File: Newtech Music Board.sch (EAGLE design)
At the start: 55 parts, among them IC1 LM386N-1, J1 SS-30_BOARD_CONNECTOR, J2 MJ-3502N, U1 74LS10N, U2 74LS174N, U3 4050N, U4 4069N, U6 78L05

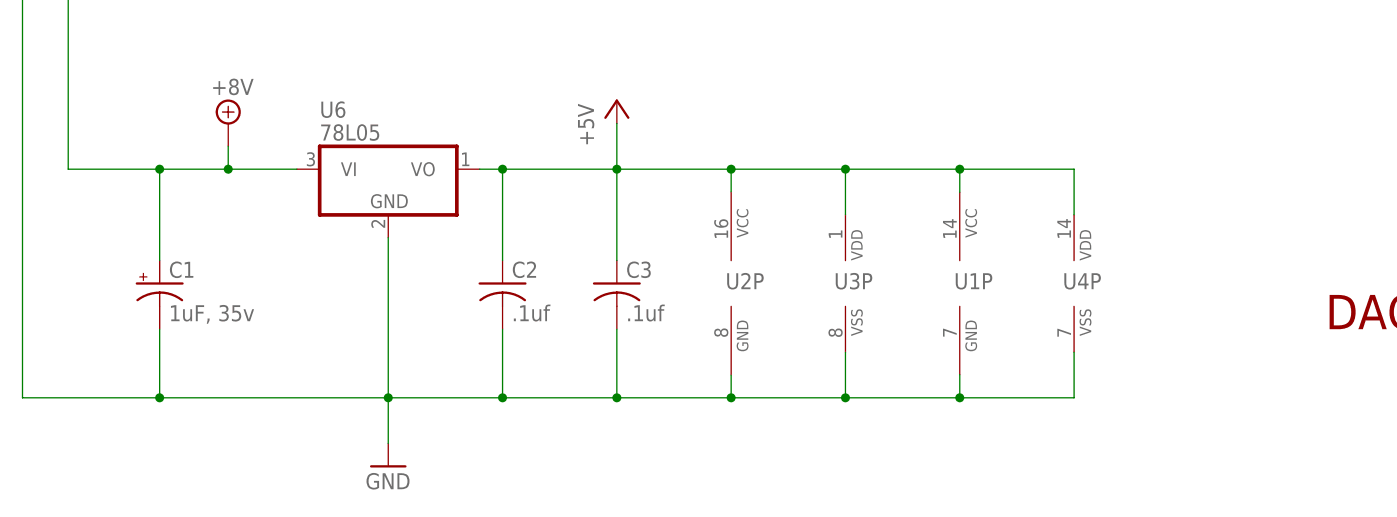
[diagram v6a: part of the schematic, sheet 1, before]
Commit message: Redid the DAC routing
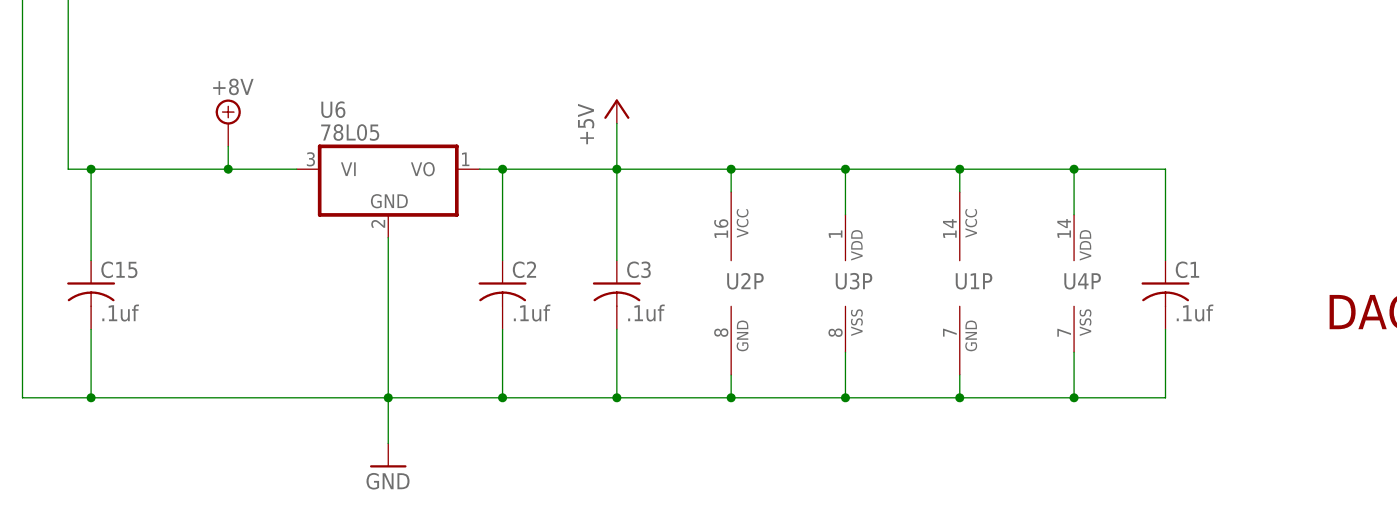
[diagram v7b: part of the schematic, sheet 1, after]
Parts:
- added C15: .1uf, rcl:C-US025-025X050
- C1: value 1uF, 35v -> .1uf; device rcl:CPOL-USE2.5-6 -> rcl:C-US025-025X050
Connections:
- net +5V: now also C1.1
- net +8V: now also C15.1; no longer C1.+
- net GND: now also C1.2, C15.2; no longer C1.-
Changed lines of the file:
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@@
 <part name="SUPPLY1" library="supply2" deviceset="+8V" device=""/>
 <part name="SUPPLY2" library="supply2" deviceset="+8V" device=""/>
-<part name="C1" library="rcl" deviceset="CPOL-US" device="E2.5-6" value="1uF, 35v"/>
 <part name="C2" library="rcl" deviceset="C-US" device="025-025X050" value=".1uf"/>
 <part name="C3" library="rcl" deviceset="C-US" device="025-025X050" value=".1uf"/>
@@
 <part name="IC1" library="linear" library_urn="urn:adsk.eagle:library:262" deviceset="LM386?-*" device="N" package3d_urn="urn:adsk.eagle:package:16409/2" technology="1"/>
 <part name="C11" library="rcl" library_urn="urn:adsk.eagle:library:334" deviceset="CPOL-US" device="E2.5-6" package3d_urn="urn:adsk.eagle:package:23349/1" value="10uF,16V"/>
+<part name="C15" library="rcl" deviceset="C-US" device="025-025X050" value=".1uf"/>
+<part name="C1" library="rcl" deviceset="C-US" device="025-025X050" value=".1uf"/>
 </parts>
 <sheets>
@@
 <attribute name="VALUE" x="28.575" y="53.975" size="1.778" layer="96"/>
 </instance>
-<instance part="C1" gate="G$1" x="22.86" y="33.02" smashed="yes">
-<attribute name="NAME" x="23.876" y="33.655" size="1.778" layer="95"/>
-<attribute name="VALUE" x="23.876" y="28.829" size="1.778" layer="96"/>
-</instance>
 <instance part="C2" gate="G$1" x="60.96" y="33.02" smashed="yes">
 <attribute name="NAME" x="61.976" y="33.655" size="1.778" layer="95"/>
@@
 <attribute name="NAME" x="40.630440625" y="51.44535" size="1.78023125" layer="95"/>
 <attribute name="VALUE" x="40.626940625" y="48.904790625" size="1.78105" layer="96"/>
+</instance>
+<instance part="C15" gate="G$1" x="15.24" y="33.02" smashed="yes">
+<attribute name="NAME" x="16.256" y="33.655" size="1.778" layer="95"/>
+<attribute name="VALUE" x="16.256" y="28.829" size="1.778" layer="96"/>
+</instance>
+<instance part="C1" gate="G$1" x="134.62" y="33.02" smashed="yes">
+<attribute name="NAME" x="135.636" y="33.655" size="1.778" layer="95"/>
+<attribute name="VALUE" x="135.636" y="28.829" size="1.778" layer="96"/>
 </instance>
 </instances>
@@
 <wire x1="15.24" y1="111.76" x2="12.7" y2="111.76" width="0.1524" layer="91"/>
 <wire x1="12.7" y1="111.76" x2="12.7" y2="45.72" width="0.1524" layer="91"/>
-<wire x1="12.7" y1="45.72" x2="22.86" y2="45.72" width="0.1524" layer="91"/>
+<wire x1="12.7" y1="45.72" x2="15.24" y2="45.72" width="0.1524" layer="91"/>
 <pinref part="J1" gate="G$2" pin="+8V@1"/>
-<wire x1="22.86" y1="45.72" x2="30.48" y2="45.72" width="0.1524" layer="91"/>
+<wire x1="15.24" y1="45.72" x2="30.48" y2="45.72" width="0.1524" layer="91"/>
 <wire x1="15.24" y1="114.3" x2="12.7" y2="114.3" width="0.1524" layer="91"/>
 <wire x1="12.7" y1="114.3" x2="12.7" y2="111.76" width="0.1524" layer="91"/>
@@
 <pinref part="SUPPLY2" gate="+8V" pin="+8V"/>
 <wire x1="30.48" y1="48.26" x2="30.48" y2="45.72" width="0.1524" layer="91"/>
-<pinref part="C1" gate="G$1" pin="+"/>
-<wire x1="22.86" y1="45.72" x2="22.86" y2="35.56" width="0.1524" layer="91"/>
-<junction x="22.86" y="45.72"/>
 <pinref part="U6" gate="G$1" pin="VI"/>
 <wire x1="30.48" y1="45.72" x2="38.1" y2="45.72" width="0.1524" layer="91"/>
 <junction x="30.48" y="45.72"/>
+<pinref part="C15" gate="G$1" pin="1"/>
+<wire x1="15.24" y1="35.56" x2="15.24" y2="45.72" width="0.1524" layer="91"/>
+<junction x="15.24" y="45.72"/>
 </segment>
 <segment>
@@
 <wire x1="60.96" y1="45.72" x2="58.42" y2="45.72" width="0.1524" layer="91"/>
 <junction x="60.96" y="45.72"/>
+<pinref part="C1" gate="G$1" pin="1"/>
+<wire x1="124.46" y1="45.72" x2="134.62" y2="45.72" width="0.1524" layer="91"/>
+<wire x1="134.62" y1="45.72" x2="134.62" y2="35.56" width="0.1524" layer="91"/>
+<junction x="124.46" y="45.72"/>
 </segment>
 <segment>
@@
 </segment>
 </net>
-<net name="GND" class="0">
+<net name="GND" class="1">
 <segment>
 <pinref part="R12" gate="G$1" pin="1"/>
@@
 <wire x1="7.62" y1="109.22" x2="7.62" y2="106.68" width="0.1524" layer="91"/>
 <wire x1="7.62" y1="106.68" x2="7.62" y2="20.32" width="0.1524" layer="91"/>
-<wire x1="7.62" y1="20.32" x2="22.86" y2="20.32" width="0.1524" layer="91"/>
 <pinref part="J1" gate="G$2" pin="GND@2"/>
-<wire x1="22.86" y1="20.32" x2="48.26" y2="20.32" width="0.1524" layer="91"/>
+<wire x1="7.62" y1="20.32" x2="15.24" y2="20.32" width="0.1524" layer="91"/>
+<wire x1="15.24" y1="20.32" x2="48.26" y2="20.32" width="0.1524" layer="91"/>
 <wire x1="15.24" y1="106.68" x2="7.62" y2="106.68" width="0.1524" layer="91"/>
 <junction x="7.62" y="106.68"/>
@@
 <wire x1="99.06" y1="20.32" x2="111.76" y2="20.32" width="0.1524" layer="91"/>
 <wire x1="86.36" y1="22.86" x2="86.36" y2="20.32" width="0.1524" layer="91"/>
-<pinref part="C1" gate="G$1" pin="-"/>
-<wire x1="22.86" y1="20.32" x2="22.86" y2="27.94" width="0.1524" layer="91"/>
 <pinref part="C2" gate="G$1" pin="2"/>
 <wire x1="60.96" y1="27.94" x2="60.96" y2="20.32" width="0.1524" layer="91"/>
 <pinref part="C3" gate="G$1" pin="2"/>
 <wire x1="73.66" y1="27.94" x2="73.66" y2="20.32" width="0.1524" layer="91"/>
-<junction x="22.86" y="20.32"/>
 <junction x="48.26" y="20.32"/>
 <junction x="60.96" y="20.32"/>
@@
 <pinref part="U6" gate="G$1" pin="GND"/>
 <wire x1="48.26" y1="38.1" x2="48.26" y2="20.32" width="0.1524" layer="91"/>
+<pinref part="C15" gate="G$1" pin="2"/>
+<wire x1="15.24" y1="27.94" x2="15.24" y2="20.32" width="0.1524" layer="91"/>
+<junction x="15.24" y="20.32"/>
+<pinref part="C1" gate="G$1" pin="2"/>
+<wire x1="134.62" y1="27.94" x2="134.62" y2="20.32" width="0.1524" layer="91"/>
+<wire x1="134.62" y1="20.32" x2="124.46" y2="20.32" width="0.1524" layer="91"/>
+<junction x="124.46" y="20.32"/>
 </segment>
 </net>
@@
 </busses>
 <nets>
-<net name="GND" class="0">
+<net name="GND" class="1">
 <segment>
 <wire x1="30.48" y1="58.42" x2="33.02" y2="55.88" width="0.1524" layer="91"/>

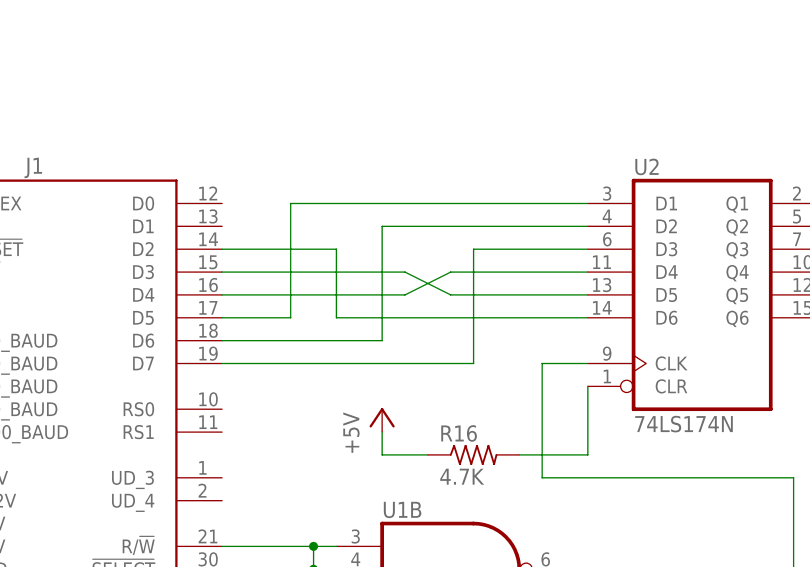
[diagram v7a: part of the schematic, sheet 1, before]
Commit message: Fixed the mixed up D7 and D5 lines
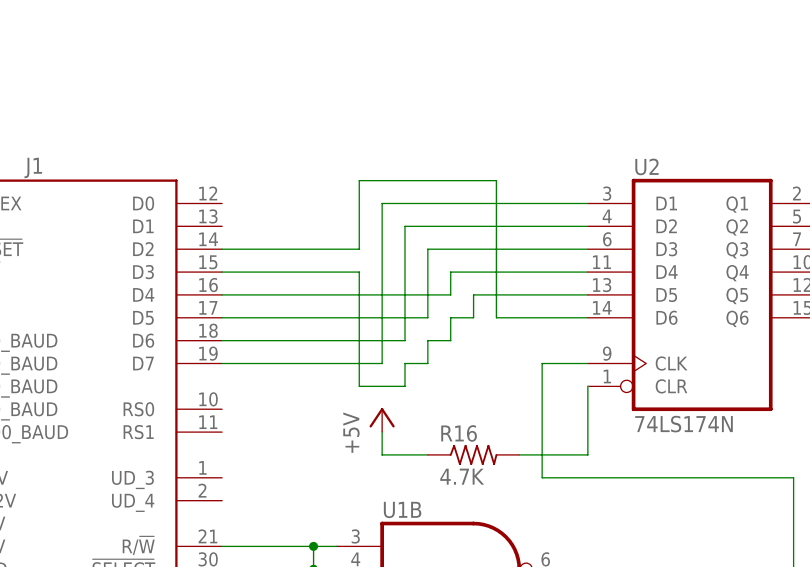
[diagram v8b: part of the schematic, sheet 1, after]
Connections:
- net N$1: now also U2A.D1; no longer U2A.D3
- net N$3: now also U2A.D3; no longer U2A.D1
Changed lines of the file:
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@@
-</segment>
-</net>
-<net name="N$1" class="0">
-<segment>
-<pinref part="U2" gate="A" pin="D3"/>
-<pinref part="J1" gate="G$2" pin="D7"/>
-<wire x1="91.44" y1="144.78" x2="78.74" y2="144.78" width="0.1524" layer="91"/>
-<wire x1="78.74" y1="144.78" x2="78.74" y2="132.08" width="0.1524" layer="91"/>
-<wire x1="78.74" y1="132.08" x2="50.8" y2="132.08" width="0.1524" layer="91"/>
-</segment>
-</net>
-<net name="N$2" class="0">
-<segment>
-<pinref part="U2" gate="A" pin="D2"/>
-<pinref part="J1" gate="G$2" pin="D6"/>
-<wire x1="91.44" y1="147.32" x2="68.58" y2="147.32" width="0.1524" layer="91"/>
-<wire x1="68.58" y1="147.32" x2="68.58" y2="134.62" width="0.1524" layer="91"/>
-<wire x1="68.58" y1="134.62" x2="50.8" y2="134.62" width="0.1524" layer="91"/>
-</segment>
-</net>
-<net name="N$3" class="0">
-<segment>
-<pinref part="U2" gate="A" pin="D1"/>
-<pinref part="J1" gate="G$2" pin="D5"/>
-<wire x1="91.44" y1="149.86" x2="58.42" y2="149.86" width="0.1524" layer="91"/>
-<wire x1="58.42" y1="149.86" x2="58.42" y2="137.16" width="0.1524" layer="91"/>
-<wire x1="58.42" y1="137.16" x2="50.8" y2="137.16" width="0.1524" layer="91"/>
-</segment>
-</net>
-<net name="N$6" class="0">
-<segment>
-<pinref part="U2" gate="A" pin="D4"/>
-<pinref part="J1" gate="G$2" pin="D4"/>
-<wire x1="91.44" y1="142.24" x2="76.2" y2="142.24" width="0.1524" layer="91"/>
-<wire x1="76.2" y1="142.24" x2="71.12" y2="139.7" width="0.1524" layer="91"/>
-<wire x1="71.12" y1="139.7" x2="50.8" y2="139.7" width="0.1524" layer="91"/>
-</segment>
-</net>
-<net name="N$7" class="0">
-<segment>
-<pinref part="U2" gate="A" pin="D5"/>
-<pinref part="J1" gate="G$2" pin="D3"/>
-<wire x1="91.44" y1="139.7" x2="76.2" y2="139.7" width="0.1524" layer="91"/>
-<wire x1="76.2" y1="139.7" x2="71.12" y2="142.24" width="0.1524" layer="91"/>
-<wire x1="71.12" y1="142.24" x2="50.8" y2="142.24" width="0.1524" layer="91"/>
-</segment>
-</net>
-<net name="N$8" class="0">
-<segment>
-<pinref part="U2" gate="A" pin="D6"/>
-<pinref part="J1" gate="G$2" pin="D2"/>
-<wire x1="91.44" y1="137.16" x2="63.5" y2="137.16" width="0.1524" layer="91"/>
-<wire x1="63.5" y1="137.16" x2="63.5" y2="144.78" width="0.1524" layer="91"/>
-<wire x1="63.5" y1="144.78" x2="50.8" y2="144.78" width="0.1524" layer="91"/>
 </segment>
 </net>
@@
 </segment>
 </net>
+<net name="N$1" class="0">
+<segment>
+<pinref part="J1" gate="G$2" pin="D7"/>
+<wire x1="50.8" y1="132.08" x2="68.58" y2="132.08" width="0.1524" layer="91"/>
+<wire x1="68.58" y1="132.08" x2="68.58" y2="149.86" width="0.1524" layer="91"/>
+<pinref part="U2" gate="A" pin="D1"/>
+<wire x1="68.58" y1="149.86" x2="91.44" y2="149.86" width="0.1524" layer="91"/>
+</segment>
+</net>
+<net name="N$2" class="0">
+<segment>
+<pinref part="J1" gate="G$2" pin="D6"/>
+<wire x1="50.8" y1="134.62" x2="71.12" y2="134.62" width="0.1524" layer="91"/>
+<wire x1="71.12" y1="134.62" x2="71.12" y2="147.32" width="0.1524" layer="91"/>
+<pinref part="U2" gate="A" pin="D2"/>
+<wire x1="71.12" y1="147.32" x2="91.44" y2="147.32" width="0.1524" layer="91"/>
+</segment>
+</net>
+<net name="N$3" class="0">
+<segment>
+<pinref part="J1" gate="G$2" pin="D5"/>
+<wire x1="50.8" y1="137.16" x2="73.66" y2="137.16" width="0.1524" layer="91"/>
+<wire x1="73.66" y1="137.16" x2="73.66" y2="144.78" width="0.1524" layer="91"/>
+<pinref part="U2" gate="A" pin="D3"/>
+<wire x1="73.66" y1="144.78" x2="91.44" y2="144.78" width="0.1524" layer="91"/>
+</segment>
+</net>
+<net name="N$6" class="0">
+<segment>
+<pinref part="J1" gate="G$2" pin="D4"/>
+<wire x1="50.8" y1="139.7" x2="76.2" y2="139.7" width="0.1524" layer="91"/>
+<wire x1="76.2" y1="139.7" x2="76.2" y2="142.24" width="0.1524" layer="91"/>
+<pinref part="U2" gate="A" pin="D4"/>
+<wire x1="76.2" y1="142.24" x2="91.44" y2="142.24" width="0.1524" layer="91"/>
+</segment>
+</net>
+<net name="N$7" class="0">
+<segment>
+<pinref part="J1" gate="G$2" pin="D3"/>
+<wire x1="50.8" y1="142.24" x2="66.04" y2="142.24" width="0.1524" layer="91"/>
+<wire x1="66.04" y1="142.24" x2="66.04" y2="129.54" width="0.1524" layer="91"/>
+<wire x1="66.04" y1="129.54" x2="71.12" y2="129.54" width="0.1524" layer="91"/>
+<wire x1="71.12" y1="129.54" x2="71.12" y2="132.08" width="0.1524" layer="91"/>
+<wire x1="71.12" y1="132.08" x2="73.66" y2="132.08" width="0.1524" layer="91"/>
+<wire x1="73.66" y1="132.08" x2="73.66" y2="134.62" width="0.1524" layer="91"/>
+<wire x1="73.66" y1="134.62" x2="76.2" y2="134.62" width="0.1524" layer="91"/>
+<wire x1="76.2" y1="134.62" x2="76.2" y2="137.16" width="0.1524" layer="91"/>
+<wire x1="76.2" y1="137.16" x2="78.74" y2="137.16" width="0.1524" layer="91"/>
+<wire x1="78.74" y1="137.16" x2="78.74" y2="139.7" width="0.1524" layer="91"/>
+<pinref part="U2" gate="A" pin="D5"/>
+<wire x1="78.74" y1="139.7" x2="91.44" y2="139.7" width="0.1524" layer="91"/>
+</segment>
+</net>
+<net name="N$8" class="0">
+<segment>
+<pinref part="J1" gate="G$2" pin="D2"/>
+<wire x1="50.8" y1="144.78" x2="66.04" y2="144.78" width="0.1524" layer="91"/>
+<wire x1="66.04" y1="144.78" x2="66.04" y2="152.4" width="0.1524" layer="91"/>
+<wire x1="66.04" y1="152.4" x2="81.28" y2="152.4" width="0.1524" layer="91"/>
+<wire x1="81.28" y1="152.4" x2="81.28" y2="137.16" width="0.1524" layer="91"/>
+<pinref part="U2" gate="A" pin="D6"/>
+<wire x1="81.28" y1="137.16" x2="91.44" y2="137.16" width="0.1524" layer="91"/>
+</segment>
+</net>
